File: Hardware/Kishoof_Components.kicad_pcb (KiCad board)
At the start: 4 copper layers, 70.8 x 110 mm, 108 parts, among them J1 SWD_Header, J10 VOct, J11 WavetablePosA, J12 WavetablePos, J13 VCA, J14 Conn_01x02_Socket, J15 Conn_01x02_Socket, J16 Conn_01x02_Socket, J17 Conn_01x02_Socket, J18 USB_C_Receptacle, J2 Eurorack_10_pin_power, J7 Audio_Out_L, J8 Audio_Out_R, J9 WarpCV, SW1 Encoder, SW2 Mode_Switch, SW3 Octave_Switch, SW4 ChB_Output, SW5 SW_Push, U1 STM32H7B0VBTx, U2 PCM5100APW, U3 TPS561201, U4 LT1117-3.3, U5 MCP6002, U6 MX25LM51245G, U7 MCP6004, U8 TL072, U9 STF202-22T1G, Y1 8MHz 20pF

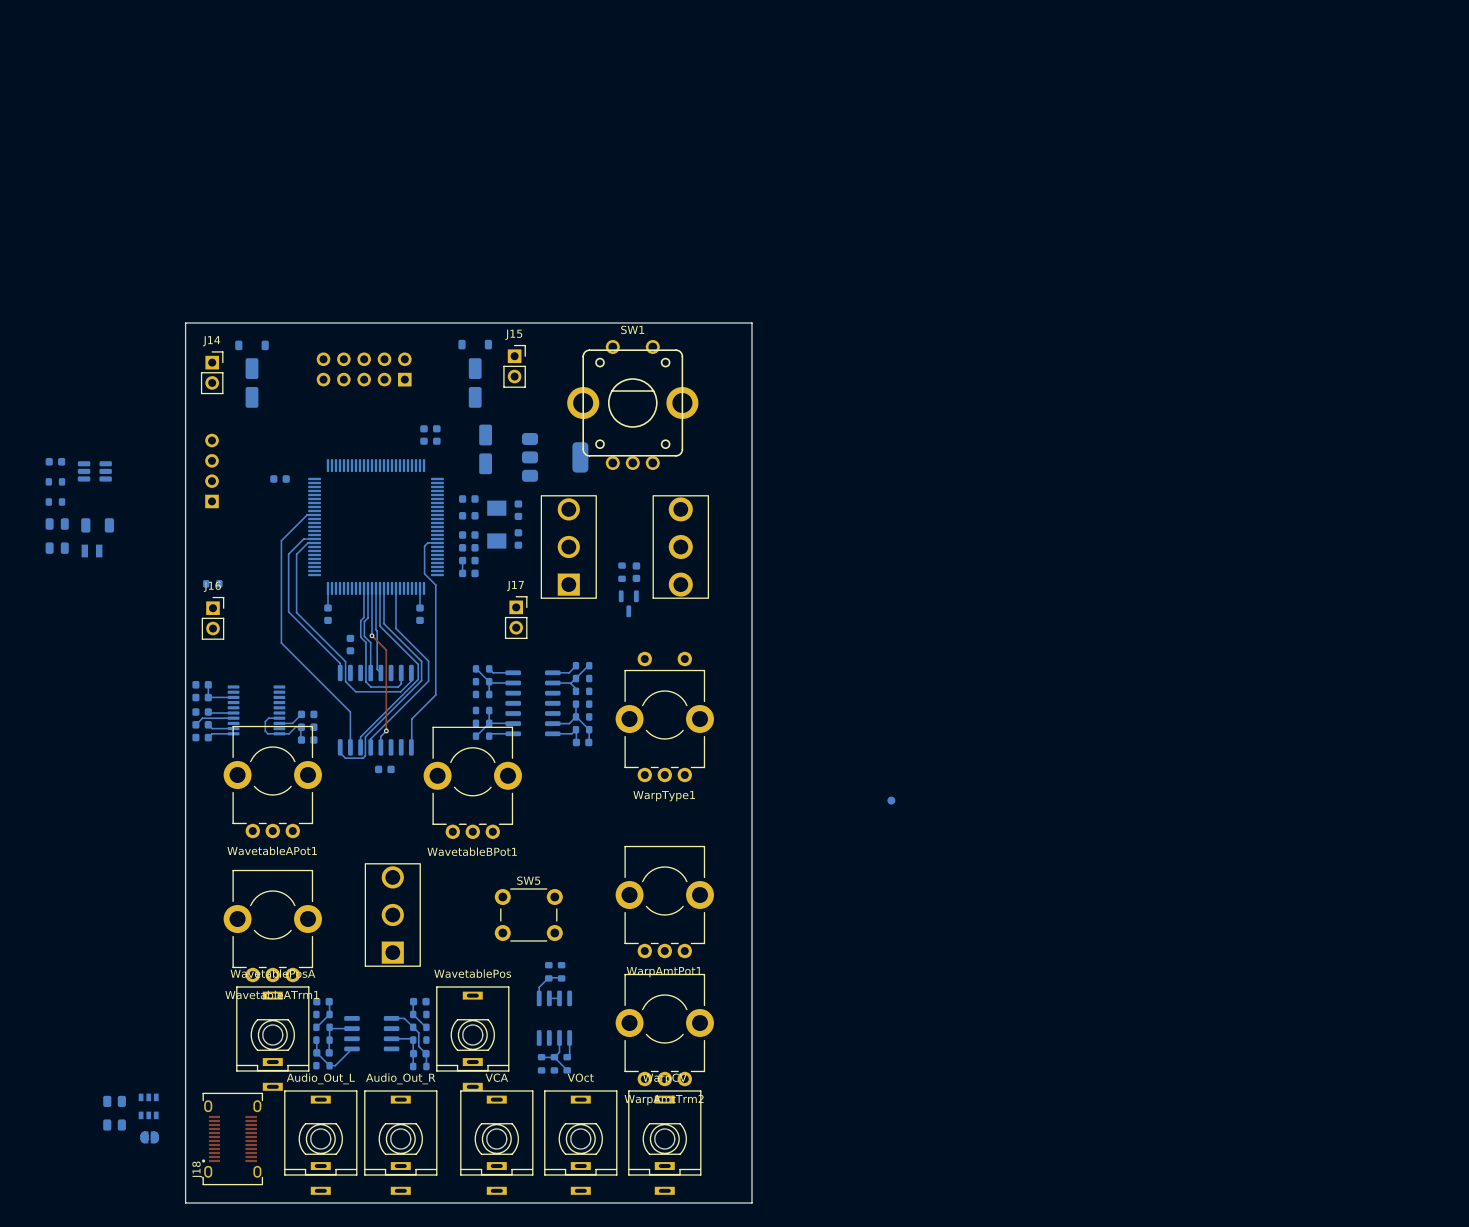
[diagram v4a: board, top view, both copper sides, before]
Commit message: First draft signal routing on component pcb
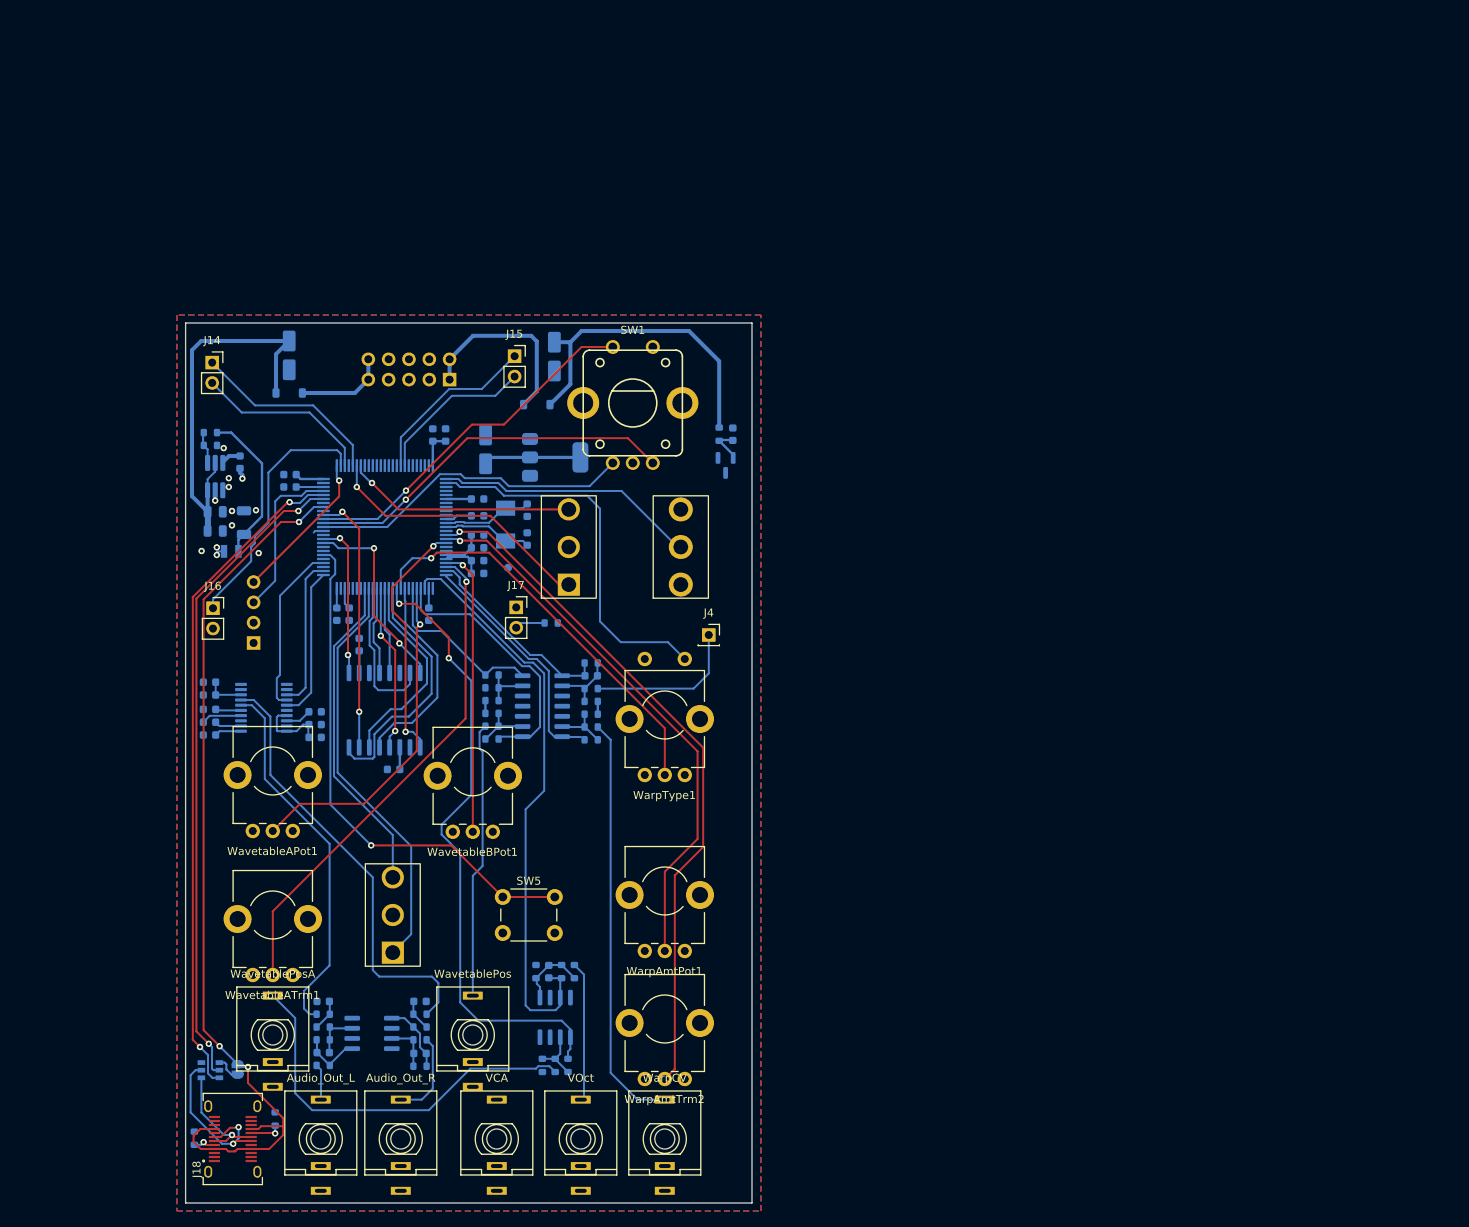
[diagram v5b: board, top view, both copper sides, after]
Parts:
- removed R30, R31: 10k, Resistor_SMD:R_0603_1608Metric
- added C37: 2.2nF, Capacitor_SMD:C_0603_1608Metric, B.Cu at (105.8, 83.1)
- added C38: 2.2uF, Capacitor_SMD:C_0603_1608Metric, B.Cu at (75.5, 75.4)
- added C39: 2.2uF, Capacitor_SMD:C_0603_1608Metric, B.Cu at (68.2, 59.5)
- added J4: Conn_01x01_Socket, Connector_PinSocket_2.54mm:PinSocket_1x01_P2.54mm_Vertical, F.Cu at (120.5, 78.0)
- added R32: 20k, Resistor_SMD:R_0603_1608Metric, B.Cu at (105.8, 86.3)
- added R33: 47k, Resistor_SMD:R_0603_1608Metric, B.Cu at (105.8, 84.7)
- added R34: 6k8, Resistor_SMD:R_0603_1608Metric, B.Cu at (105.8, 81.5)
- C29, C30: value 2n2 -> 2.2nF
- C35: value 1.5nF -> 2.2nF
- R28, R29: footprint Resistor_SMD:R_0805_2012Metric -> Resistor_SMD:R_0603_1608Metric
- U3: footprint Package_TO_SOT_SMD:SOT-23-6_Handsoldering -> Package_TO_SOT_SMD:TSOT-23-6_HandSoldering
- moved TP1 56.1 mm to (95.4, 69.6)
- moved R19 50.0 mm to (102.9, 131.8), turned to -90 degrees
- moved R27 49.5 mm to (93.4, 83.0), turned to 0 degrees
- moved R17 48.5 mm to (101.3, 131.8), turned to -90 degrees
- moved R26 47.4 mm to (93.4, 84.6), turned to 180 degrees
- moved R16 47.0 mm to (99.7, 131.8), turned to -90 degrees
- moved R25 46.1 mm to (93.4, 86.2), turned to 180 degrees
- moved R15 42.6 mm to (100.8, 76.5)
- moved R24 39.1 mm to (102.1, 120.1), turned to 90 degrees
- moved R23 38.0 mm to (103.7, 120.1), turned to 90 degrees
- moved R22 35.3 mm to (98.9, 120.1), turned to 90 degrees
- moved C35 28.9 mm to (100.5, 120.1), turned to 90 degrees
- moved C8 23.1 mm to (61.9, 56.4), turned to 90 degrees
- moved D3 21.1 mm to (122.6, 56.8)
- moved R14 21.1 mm to (121.8, 52.9)
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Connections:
- C13 pad 1: +3V3 -> +3.3V
- C28 pad 1: +3V3 -> +3.3V
- C33 pad 1: +3V3 -> +3.3V
- C34 pad 1: +3V3 -> +3.3V
- C35 pad 2: Net-(U7B--) -> Net-(U5B-+)
- J14 pad 1: /LCD_SPI3_SCK -> /LCD_SPI3_MOSI
- J14 pad 2: /LCD_SPI3_MOSI -> /LCD_SPI3_SCK
- J16 pad 1: /LCD_BACKLIGHT -> /LCD_SPI3_SS
- J16 pad 2: /LCD_SPI3_SS -> GND
- J17 pad 2: GND -> /LCD_BACKLIGHT
- J18 pad A4: /VBUS -> /USB_VBUS
- J18 pad A9: /VBUS -> /USB_VBUS
- J18 pad B4: /VBUS -> /USB_VBUS
- J18 pad B9: /VBUS -> /USB_VBUS
- JP1 pad 2: /VBUS -> /USB_VBUS
- R13 pad 1: /Pitch_CV_Scaled -> /WarpCV
- R16 pad 1: Net-(U7A--) -> Net-(U5A--)
- R17 pad 1: Net-(U7A--) -> Net-(U5A--)
- R19 pad 2: Net-(U7A--) -> Net-(U5A--)
- R20 pad 2: /PITCH_CV -> /WARP_CV
- R22 pad 1: Net-(U7D--) -> Net-(U5B-+)
- R23 pad 1: Net-(U7D--) -> Net-(U5B-+)
- R23 pad 2: /WARP_CV -> /PITCH_CV
- R24 pad 1: /WarpCV -> /Pitch_CV_Scaled
- R24 pad 2: Net-(U7D--) -> Net-(U5B-+)
- R25 pad 1: Net-(U5A--) -> Net-(U7D--)
- R26 pad 1: Net-(U5A--) -> Net-(U7D--)
- R27 pad 2: Net-(U5A--) -> Net-(U7D--)
- U1 pad 1: unconnected-(U1-PE2-Pad1) -> /Mode
- U1 pad 16: /WAVETABLE_POS_A_TRM -> /WARP_AMT_POT
- U1 pad 2: unconnected-(U1-PE3-Pad2) -> /Warp_Polarity_Btn
- U1 pad 22: /WAVETABLE_POS_A_POT -> /WAVETABLE_POS_B_POT
- U1 pad 23: /WAVETABLE_POS_B_POT -> /WAVETABLE_POS_A_TRM
- U1 pad 24: /Pitch_CV_Scaled -> /AudioIn
- U1 pad 25: /WavetablePosA_CV -> /WarpCV
- U1 pad 28: /WavetablePosB_CV -> /Pitch_CV_Scaled
- U1 pad 29: /WarpCV -> /WavetablePosB_CV
- U1 pad 30: /WARP_AMT_POT -> /WAVETABLE_POS_A_POT
- U1 pad 35: unconnected-(U1-PB1-Pad35) -> /WavetablePosA_CV
- U1 pad 44: /WARP_BIPOLAR -> unconnected-(U1-PE14-Pad44)
- U1 pad 45: /Mode -> unconnected-(U1-PE15-Pad45)
- U1 pad 48: unconnected-(U1-VCAP-Pad48) -> Net-(C38-Pad1)
- U1 pad 56: unconnected-(U1-PD9-Pad56) -> /B_Octave_Btn1
- U1 pad 62: /B_Octave_Btn1 -> unconnected-(U1-PD15-Pad62)
- U1 pad 73: unconnected-(U1-VCAP-Pad73) -> Net-(C39-Pad1)
- U1 pad 8: /LCD_DC -> unconnected-(U1-PC14-Pad8)
- U1 pad 9: /LCD_RESET -> unconnected-(U1-PC15-Pad9)
- U1 pad 92: /Warp_Polarity_Btn -> /LCD_DC
- U1 pad 93: unconnected-(U1-PB7-Pad93) -> /LCD_RESET
- U2 pad 17: +3V3 -> +3.3V
- U2 pad 20: +3V3 -> +3.3V
- U5 pad 1: /VcaCV -> /WavetablePosA_CV
- U5 pad 6: Net-(U5B--) -> GND
- U5 pad 7: Net-(U5B--) -> /Pitch_CV_Scaled
- U6 pad 11: +3V3 -> +3.3V
- U6 pad 2: +3V3 -> +3.3V
- U7 pad 1: /WavetablePosA_CV -> /AudioIn
- U7 pad 14: /WarpCV -> /VcaCV
- U7 pad 7: /Pitch_CV_Scaled -> /WarpCV
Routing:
- net /USB_VBUS: track 0.00 -> 111.8 mm, vias 0 -> 3
- net /WARP_AMT_TRM: track 0.00 -> 86.9 mm, vias 0 -> 1
- net /USB_DP: track 0.00 -> 83.7 mm, vias 0 -> 2
- net /USB_DM: track 0.00 -> 81.6 mm, vias 0 -> 2
- net /WavetablePosA_CV: track 3.38 -> 78.2 mm, vias 0 -> 2
- net /WARP_AMT_POT: track 0.00 -> 69.1 mm, vias 0 -> 1
- net /Pitch_CV_Scaled: track 4.73 -> 73.1 mm
- net /B_Octave_Btn1: track 0.00 -> 65.4 mm, vias 0 -> 1
- net /WAVETABLE_POS_A_TRM: track 0.00 -> 62.7 mm, vias 0 -> 1
- net /DAC_Out_R: track 0.00 -> 54.9 mm
- net /WARP_CV: track 0.00 -> 52.1 mm
- net /ChB_Mix: track 0.00 -> 51.9 mm
- net /Warp_Type_Pot: track 0.00 -> 51.2 mm, vias 0 -> 1
- net +12V: track 0.00 -> 49.4 mm
- net /WAVETABLE_POS_A_CV: track 0.00 -> 49.3 mm
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- added copper zone on In2.Cu, net /VSW
- added copper zone on B.Cu, net GND
- added copper zone on F.Cu, net GND
- added copper zone on In1.Cu, net GND
- added copper zone on In2.Cu, net GND

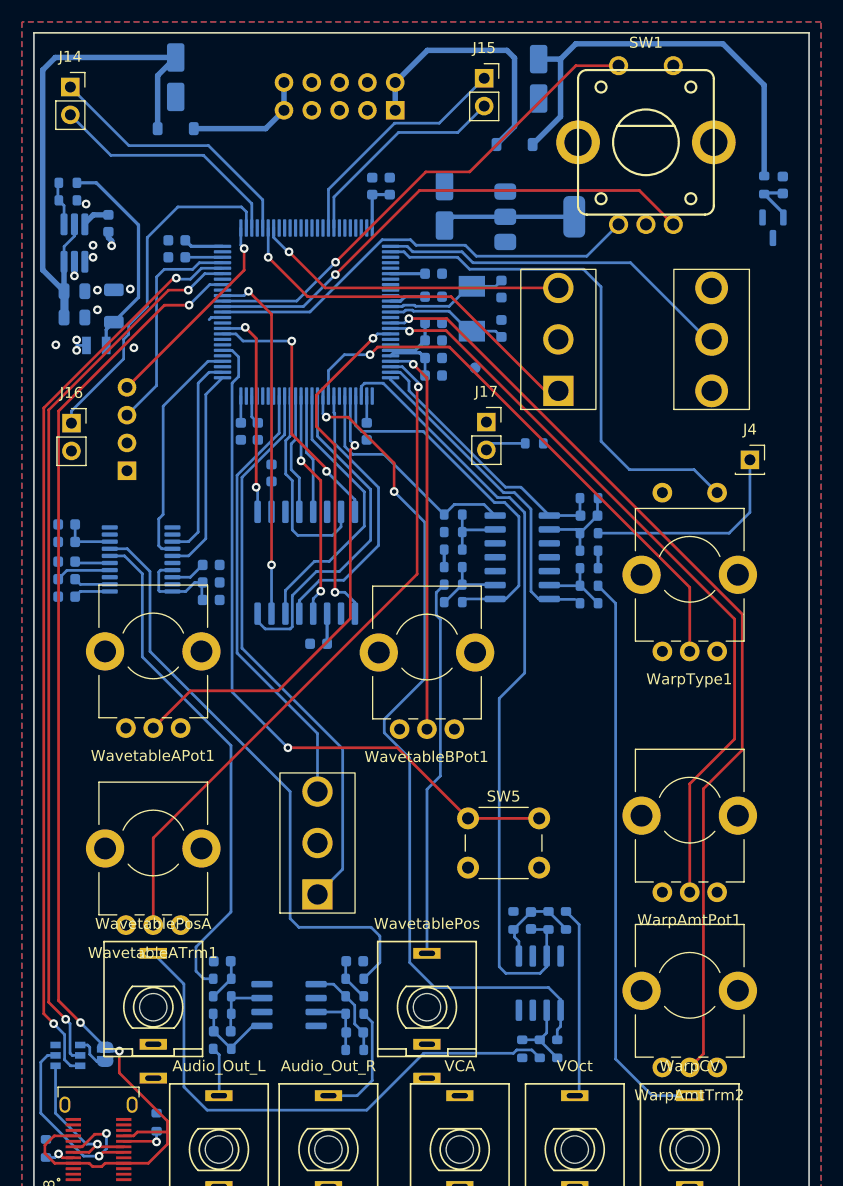
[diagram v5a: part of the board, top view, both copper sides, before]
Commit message: Started routing power
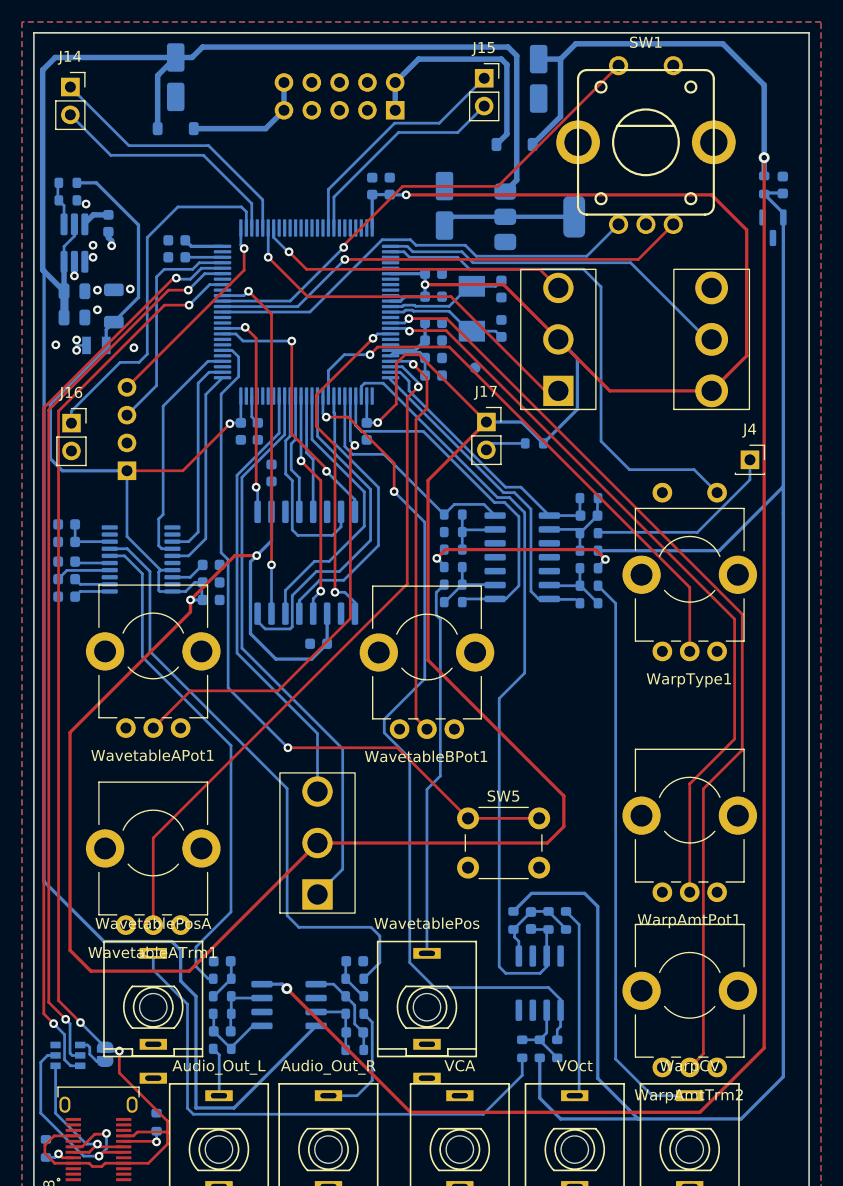
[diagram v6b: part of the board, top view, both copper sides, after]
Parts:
- moved R16 1.60 mm to (101.3, 131.8)
- moved R17 1.60 mm to (99.7, 131.8)
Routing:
- net +3.3V: track 53.8 -> 376.8 mm, vias 0 -> 6
- net /-5V_REF: track 7.95 -> 180.1 mm, vias 0 -> 2
- net +12V: track 49.4 -> 194.0 mm
- net -12V: track 39.9 -> 174.4 mm, vias 0 -> 2
- net /ENCODER_DN: track 46.8 -> 44.3 mm
- net /-12V_IN: track 23.5 -> 21.5 mm
- net /EXT_AUDIO_IN: track 19.5 -> 17.7 mm
- net unconnected-(U1-PD15-Pad62): track 1.31 -> 0.00 mm
- net /LCD_SPI3_SS: track 31.7 -> 32.7 mm
- net /WAVETABLE_POS_B_POT: track 36.0 -> 36.9 mm
- net /B_Octave_Btn1: track 65.4 -> 66.2 mm
